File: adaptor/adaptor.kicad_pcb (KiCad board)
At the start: 2 copper layers, 2 parts, among them CN1 XT30(2+2)PB-M.G.B, CN2 XT30(2+2)PB-M.G.B

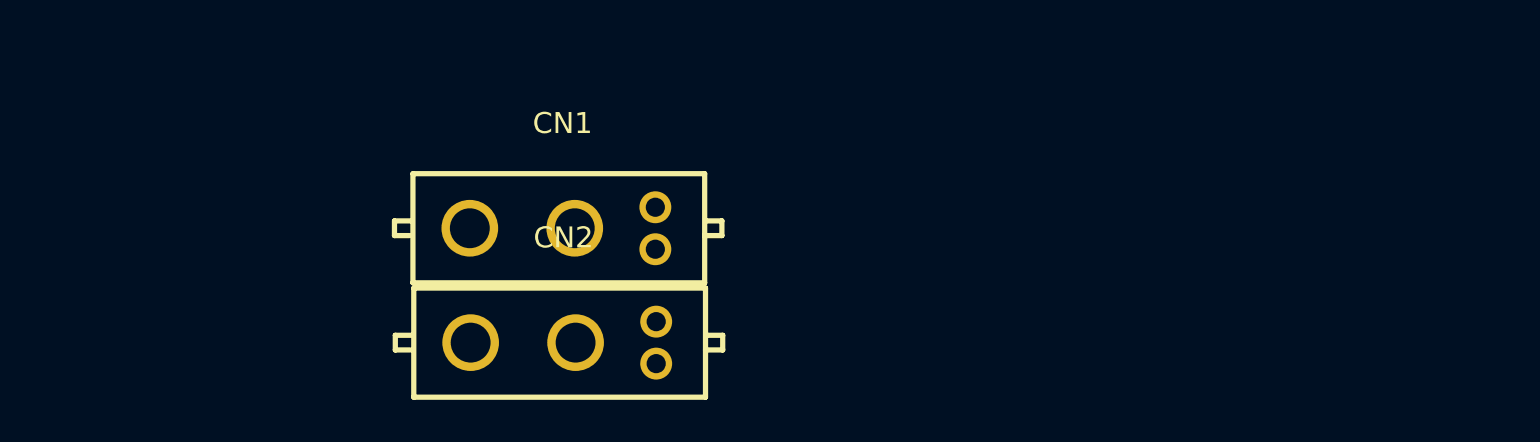
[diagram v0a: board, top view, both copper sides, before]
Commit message: [Hw] Rough adaptor board layout, and form factor
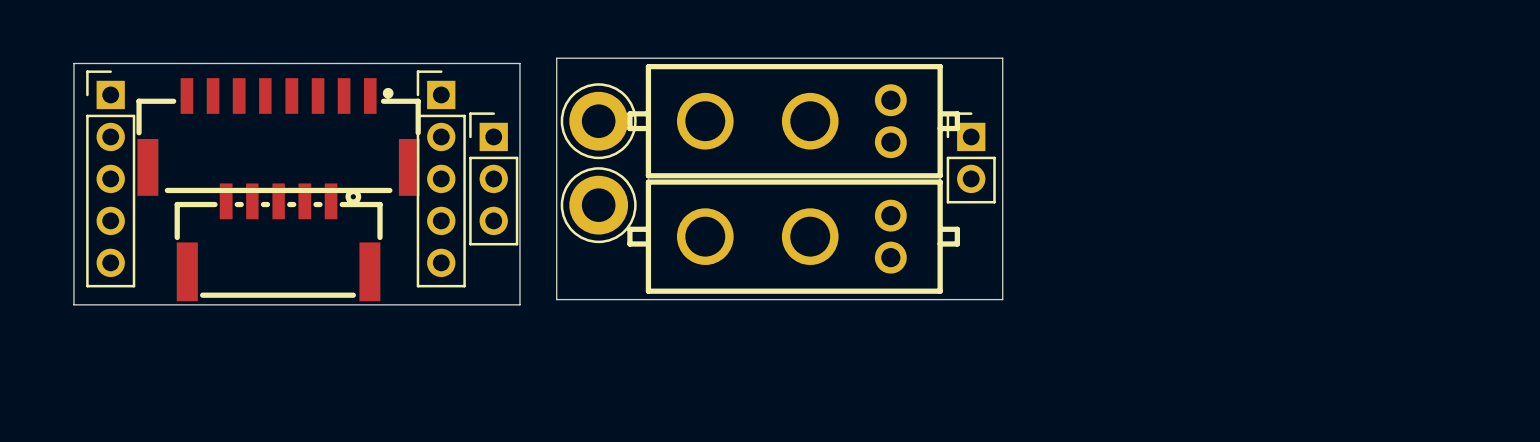
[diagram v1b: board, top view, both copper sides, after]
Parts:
- added CN3: BM08B-GHS-TBT(LF)(SN)_C133062, easyeda:CONN-SMD_BM08B-GHS-TBT-LF-SN, F.Cu at (125.2, 97.8)
- added CN4: BM05B-GHS-TBT(LF)(SN)(N), easyeda:CONN-SMD_BM05B-GHS-TBT, F.Cu at (125.2, 102.8)
- added H1: ~, TestPoint:TestPoint_Keystone_5005-5009_Compact, F.Cu at (140.5, 101.2)
- added H2: ~, TestPoint:TestPoint_Keystone_5005-5009_Compact, F.Cu at (140.5, 97.2)
- added J1: Conn_01x05_Socket, Connector_PinHeader_2.00mm:PinHeader_1x05_P2.00mm_Vertical, F.Cu at (117.2, 96.0)
- added J2: Conn_01x05_Socket, Connector_PinHeader_2.00mm:PinHeader_1x05_P2.00mm_Vertical, F.Cu at (133.0, 96.0)
- added J3: ~, Connector_PinHeader_2.00mm:PinHeader_1x02_P2.00mm_Vertical, F.Cu at (158.2, 98.0)
- added J4: Conn_01x05_Socket, Connector_PinHeader_2.00mm:PinHeader_1x03_P2.00mm_Vertical, F.Cu at (135.5, 98.0)
- moved CN1 12.3 mm to (150.0, 97.2)
- moved CN2 12.3 mm to (150.0, 102.8)
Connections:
- CN1 pad 1: unconnected-(CN1-Pad1) -> Net-(J3-Pin_1)
- CN1 pad 2: unconnected-(CN1-Pad2) -> Net-(J3-Pin_2)
- CN1 pad 3: unconnected-(CN1-Pad3) -> Net-(CN1-Pad3)
- CN1 pad 4: unconnected-(CN1-Pad4) -> Net-(CN1-Pad4)
- CN2 pad 1: unconnected-(CN2-Pad1) -> Net-(J3-Pin_1)
- CN2 pad 2: unconnected-(CN2-Pad2) -> Net-(J3-Pin_2)
- CN2 pad 3: unconnected-(CN2-Pad3) -> Net-(CN1-Pad3)
- CN2 pad 4: unconnected-(CN2-Pad4) -> Net-(CN1-Pad4)
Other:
- board outline added: 44.2 x 11.8 mm

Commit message: Adaptor boards
- CAN/Power XT30 2+2
- Break out Aux ports to 10 and 8 pin jst GH
- AS5046D encoder board with 10 pin jst GH connector

Signed-off-by: Will Haarhoff <williamhaarhoff@gmail.com>
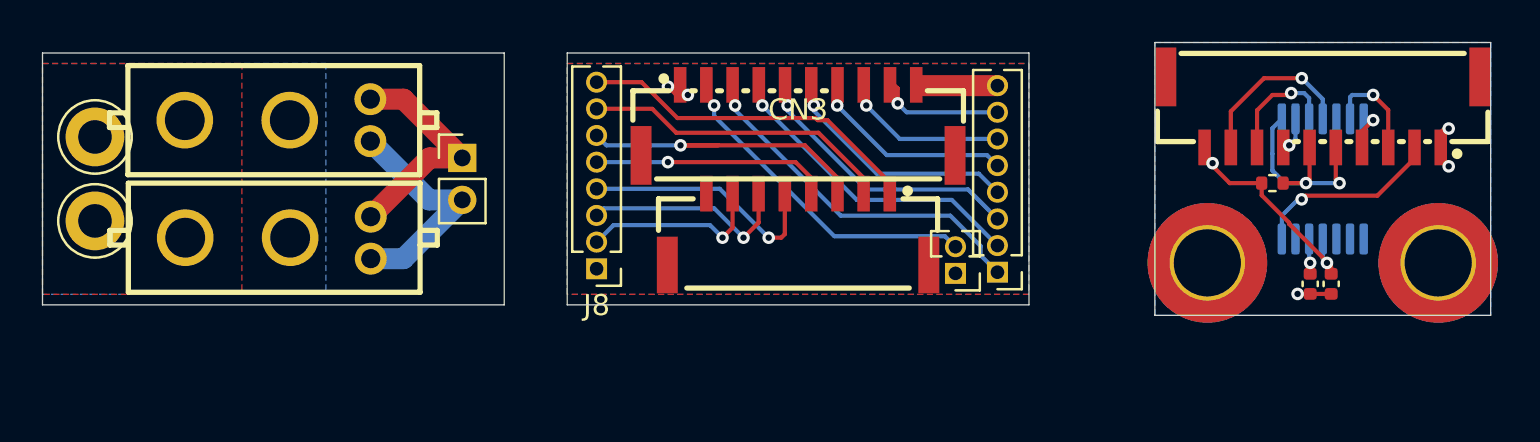
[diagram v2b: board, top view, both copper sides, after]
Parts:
- removed CN4: BM05B-GHS-TBT(LF)(SN)(N), easyeda:CONN-SMD_BM05B-GHS-TBT
- removed J1, J2: Conn_01x05_Socket, Connector_PinHeader_2.00mm:PinHeader_1x05_P2.00mm_Vertical
- added C18: 1u, Capacitor_SMD:C_0402_1005Metric, F.Cu at (174.4, 105.0)
- added C24: 100n, Capacitor_SMD:C_0402_1005Metric, F.Cu at (175.4, 105.0)
- added CN5: WAFER-GH1.25-10PLB, easyeda:CONN-SMD_10P-P1.25_XUNPU_WAFER-GH1.25-10PLB, F.Cu at (150.0, 97.2)
- added CN6: WAFER-GH1.25-10PLB, easyeda:CONN-SMD_10P-P1.25_XUNPU_WAFER-GH1.25-10PLB, F.Cu at (175.0, 96.8)
- added H3: MountingHole_Pad, MountingHole:MountingHole_3.2mm_M3_ISO7380_Pad_TopBottom, F.Cu at (169.5, 104.0)
- added H4: MountingHole_Pad, MountingHole:MountingHole_3.2mm_M3_ISO7380_Pad_TopBottom, F.Cu at (180.5, 104.0)
- added J7: Conn_01x08_Socket, Connector_PinHeader_1.27mm:PinHeader_1x08_P1.27mm_Vertical, F.Cu at (159.5, 104.4)
- added J8: Conn_01x08_Socket, Connector_PinHeader_1.27mm:PinHeader_1x08_P1.27mm_Vertical, F.Cu at (140.4, 104.3)
- added R5: 10k, Resistor_SMD:R_0402_1005Metric, F.Cu at (172.6, 100.2)
- added U5: AS5047D, Package_SO:TSSOP-14_4.4x5mm_P0.65mm, B.Cu at (175.0, 100.0)
- J4: value Conn_01x05_Socket -> Conn_01x02_Socket; footprint Connector_PinHeader_2.00mm:PinHeader_1x03_P2.00mm_Vertical -> Connector_PinHeader_1.27mm:PinHeader_1x02_P1.27mm_Vertical
- moved CN3 25.2 mm to (150.0, 102.4)
- moved CN1 24.8 mm to (125.2, 97.2)
- moved CN2 24.8 mm to (125.2, 102.8)
- moved J3 24.3 mm to (134.0, 99.0)
- moved H1 24.0 mm to (116.5, 102.0)
- moved H2 24.0 mm to (116.5, 98.0)
- moved J4 22.9 mm to (157.5, 104.5), turned to 180 degrees
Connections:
- CN3 pad 1: Net-(J2-Pin_1) -> Net-(J8-Pin_8)
- CN3 pad 10: Net-(J2-Pin_1) -> unconnected-(CN3-Pad10)
- CN3 pad 6: Net-(J4-Pin_1) -> Net-(J8-Pin_3)
- CN3 pad 7: Net-(J4-Pin_2) -> Net-(J8-Pin_2)
- CN3 pad 8: Net-(J4-Pin_3) -> GND
- CN3 pad 9: Net-(J4-Pin_3) -> unconnected-(CN3-Pad9)
- J4 pad 1: Net-(J4-Pin_1) -> GND
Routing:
- net Net-(J7-Pin_1): track 0.00 -> 17.4 mm, vias 0 -> 1
- net Net-(J8-Pin_8): track 0.00 -> 16.3 mm
- net Net-(J4-Pin_2): track 0.00 -> 15.9 mm, vias 0 -> 1
- net Net-(J7-Pin_2): track 0.00 -> 15.2 mm, vias 0 -> 1
- net Net-(J8-Pin_6): track 0.00 -> 14.7 mm, vias 0 -> 1
- net Net-(J8-Pin_7): track 0.00 -> 14.6 mm
- net Net-(J7-Pin_3): track 0.00 -> 13.6 mm, vias 0 -> 1
- net Net-(J8-Pin_4): track 0.00 -> 12.1 mm, vias 0 -> 1
- net Net-(J7-Pin_4): track 0.00 -> 11.8 mm, vias 0 -> 1
- net Net-(J8-Pin_5): track 0.00 -> 11.1 mm, vias 0 -> 1
- net Net-(J3-Pin_2): track 0.00 -> 11.1 mm
- net Net-(J3-Pin_1): track 0.00 -> 11.1 mm
- net /~{NSS1}: track 0.00 -> 10.7 mm, vias 0 -> 2
- net +5V: track 0.00 -> 10.7 mm, vias 0 -> 2
- net Net-(J8-Pin_3): track 0.00 -> 10.3 mm, vias 0 -> 1
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- added copper zone on B.Cu, net GND
- added copper zone on F.Cu, net GND
- added copper zone on B.Cu, net Net-(CN1-Pad3)
- added copper zone on F.Cu, net Net-(CN1-Pad4)
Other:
- board size 44.2 x 11.8 mm -> 69 x 13 mm

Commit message: [Hw] Finished adaptor board, passes DRC
Signed-off-by: Will Haarhoff <williamhaarhoff@gmail.com>
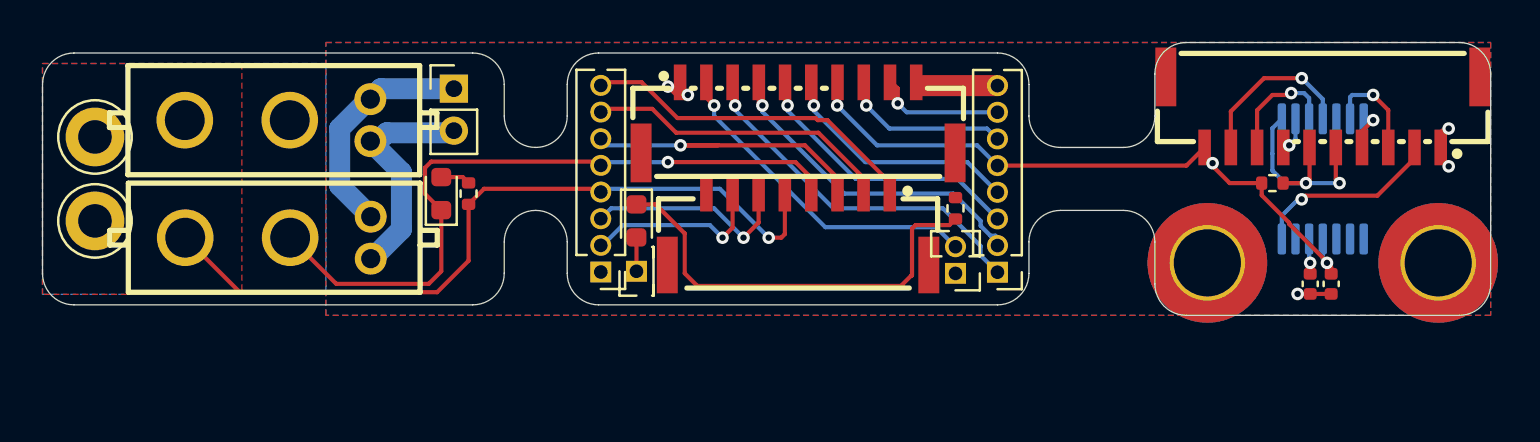
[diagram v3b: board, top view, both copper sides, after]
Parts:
- added D5: WHITE, LED_SMD:LED_0603_1608Metric, F.Cu at (142.3, 102.0)
- added D7: GREEN, LED_SMD:LED_0603_1608Metric, F.Cu at (133.0, 100.7)
- added J5: Conn_01x02_Socket, Connector_PinHeader_1.27mm:PinHeader_1x01_P1.27mm_Vertical, F.Cu at (142.3, 104.4)
- added R7: 20k, Resistor_SMD:R_0402_1005Metric, F.Cu at (134.3, 100.7)
- added R9: 20k, Resistor_SMD:R_0402_1005Metric, F.Cu at (157.5, 101.4)
- moved J3 3.32 mm to (133.6, 95.7)
- moved J8 0.25 mm to (140.6, 104.4)
- moved CN5 0.12 mm to (150.0, 97.1)
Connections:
- CN1 pad 3: Net-(CN1-Pad3) -> /DUMMY2
- CN1 pad 4: Net-(CN1-Pad4) -> /DUMMY1
- CN2 pad 3: Net-(CN1-Pad3) -> /DUMMY2
- CN2 pad 4: Net-(CN1-Pad4) -> /DUMMY1
- CN3 pad 4: Net-(J8-Pin_5) -> /DUMMY2
- CN3 pad 5: Net-(J8-Pin_4) -> /DUMMY1
- CN5 pad 7: Net-(J7-Pin_5) -> +5V
- H1 pad 1: Net-(CN1-Pad3) -> /DUMMY2
- H2 pad 1: Net-(CN1-Pad4) -> /DUMMY1
- J7 pad 5: Net-(J7-Pin_5) -> +5V
- J8 pad 4: Net-(J8-Pin_4) -> /DUMMY1
- J8 pad 5: Net-(J8-Pin_5) -> /DUMMY2
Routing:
- net /DUMMY1: track 0.00 -> 36.4 mm, vias 0 -> 1
- net /DUMMY2: track 0.00 -> 33.0 mm, vias 0 -> 1
- net Net-(D5-K): track 0.00 -> 20.6 mm
- net +5V: track 10.7 -> 31.0 mm, vias 2 -> 3
- net Net-(J8-Pin_4): track 12.1 -> 0.00 mm, vias 1 -> 0
- net Net-(J8-Pin_5): track 11.1 -> 0.00 mm, vias 1 -> 0
- net Net-(J7-Pin_5): track 10.0 -> 0.00 mm, vias 1 -> 0
- net Net-(D5-A): track 0.00 -> 1.61 mm
- net Net-(D7-A): track 0.00 -> 1.41 mm
- net Net-(J7-Pin_2): track 15.2 -> 15.8 mm
- added copper zone on F.Cu, net /DUMMY1
- added copper zone on B.Cu, net /DUMMY2
- removed copper zone on B.Cu, net Net-(CN1-Pad3)
- removed copper zone on F.Cu, net Net-(CN1-Pad4)
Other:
- outline, holes or cut-outs redrawn
